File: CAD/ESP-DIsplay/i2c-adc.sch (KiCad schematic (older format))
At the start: 1 part, among them J801 ADC_Conn

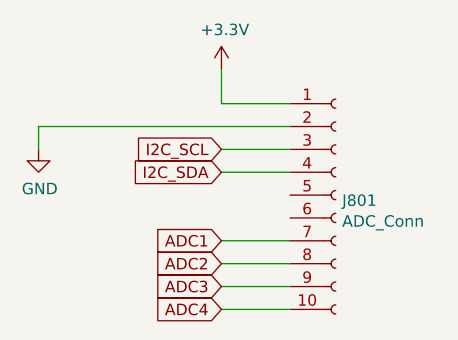
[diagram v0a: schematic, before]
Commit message: esp12e adc pinsadded, 1117 power module
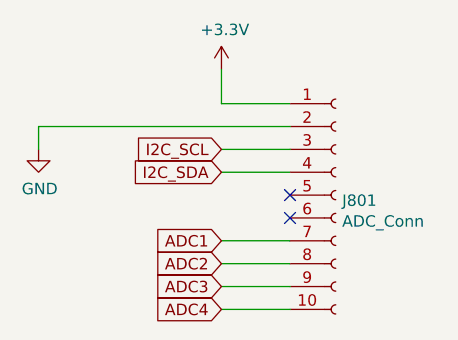
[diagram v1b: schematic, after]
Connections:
- no-connect marks 0 -> 2
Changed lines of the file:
@@
 Wire Wire Line
 	5900 3400 6200 3400
+NoConn ~ 6200 2900
+NoConn ~ 6200 3000
 $EndSCHEMATC
